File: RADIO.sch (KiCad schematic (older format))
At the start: 20 parts, among them Q501 MMBF170, U501 SN74AVC2T244, U502 SN74AVC2T244, U503 SN74AVC2T244, U504 A7, U505 SIM_SLOT, U506 SN74AVC2T244

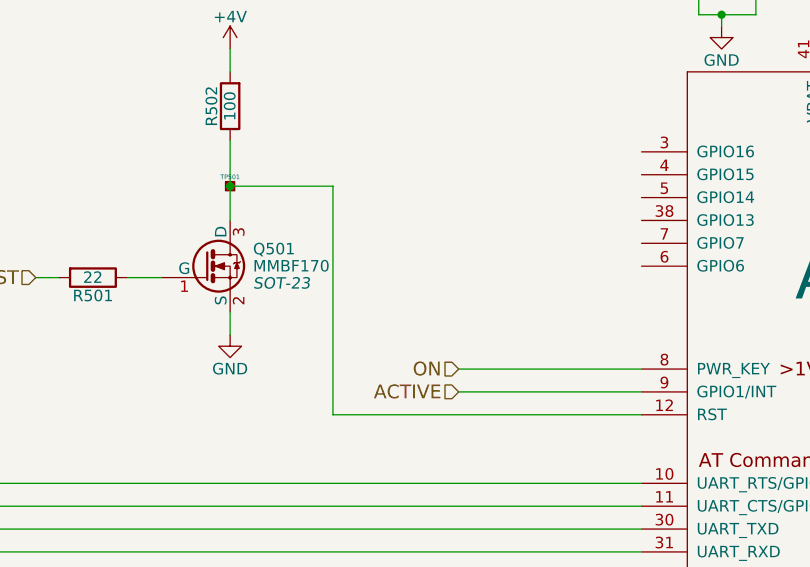
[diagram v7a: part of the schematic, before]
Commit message: Created netlist with current components Foreward Annotation to Board
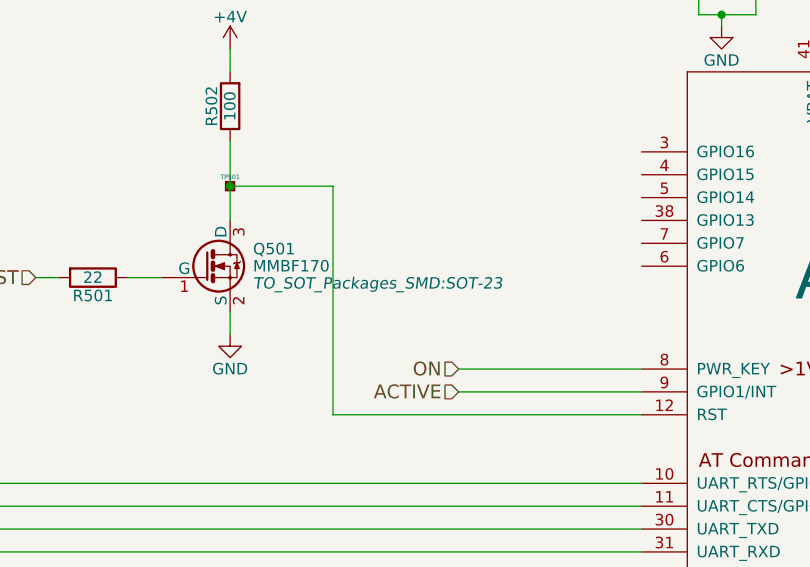
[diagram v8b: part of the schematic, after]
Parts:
- C501, C503, C504, C505, C506, C507: footprint Capacitors_SMD:C_0603 -> Capacitors_SMD:C_0402
- Q501: footprint SOT-23 -> TO_SOT_Packages_SMD:SOT-23
- R501, R502, R503, R504, R505: footprint Resistors_SMD:R_0603 -> Resistors_SMD:R_0402
- TP501: footprint buttons:TP -> NokiaRetroFit:TP
- U504: footprint buttons:A7 -> NokiaRetroFit:A7
- U505: footprint buttons:SIM -> NokiaRetroFit:SIM
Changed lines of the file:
@@
 F 0 "U504" H 10300 5750 60  0000 C CNN
 F 1 "A7" H 9700 4950 197 0000 C CNN
-F 2 "buttons:A7" H 9450 4650 60  0001 C CNN
+F 2 "NokiaRetroFit:A7" H 9450 4650 60  0001 C CNN
 F 3 "" H 9450 4650 60  0000 C CNN
 	1    9700 4450
@@
 F 0 "R501" V 6530 3950 50  0000 C CNN
 F 1 "22" V 6450 3950 50  0000 C CNN
-F 2 "Resistors_SMD:R_0603" V 6380 3950 50  0001 C CNN
+F 2 "Resistors_SMD:R_0402" V 6380 3950 50  0001 C CNN
 F 3 "" H 6450 3950 50  0000 C CNN
 	1    6450 3950
@@
 F 0 "R502" V 7130 3200 50  0000 C CNN
 F 1 "100" V 7050 3200 50  0000 C CNN
-F 2 "Resistors_SMD:R_0603" V 6980 3200 50  0001 C CNN
+F 2 "Resistors_SMD:R_0402" V 6980 3200 50  0001 C CNN
 F 3 "" H 7050 3200 50  0000 C CNN
 	1    7050 3200
@@
 F 0 "R504" V 11480 3900 50  0000 C CNN
 F 1 "0" V 11400 3900 50  0000 C CNN
-F 2 "Resistors_SMD:R_0603" V 11330 3900 50  0001 C CNN
+F 2 "Resistors_SMD:R_0402" V 11330 3900 50  0001 C CNN
 F 3 "" H 11400 3900 50  0000 C CNN
 	1    11400 3900
@@
 F 0 "C505" H 11160 4170 50  0000 L CNN
 F 1 "C" H 11160 4020 50  0000 L CNN
-F 2 "Capacitors_SMD:C_0603" H 11150 4100 50  0001 C CNN
+F 2 "Capacitors_SMD:C_0402" H 11150 4100 50  0001 C CNN
 F 3 "" H 11150 4100 50  0000 C CNN
 	1    11150 4100
@@
 F 0 "C507" H 11660 4170 50  0000 L CNN
 F 1 "C" H 11660 4020 50  0000 L CNN
-F 2 "Capacitors_SMD:C_0603" H 11650 4100 50  0001 C CNN
+F 2 "Capacitors_SMD:C_0402" H 11650 4100 50  0001 C CNN
 F 3 "" H 11650 4100 50  0000 C CNN
 	1    11650 4100
@@
 F 0 "R503" V 11480 3000 50  0000 C CNN
 F 1 "0" V 11400 3000 50  0000 C CNN
-F 2 "Resistors_SMD:R_0603" V 11330 3000 50  0001 C CNN
+F 2 "Resistors_SMD:R_0402" V 11330 3000 50  0001 C CNN
 F 3 "" H 11400 3000 50  0000 C CNN
 	1    11400 3000
@@
 F 0 "C504" H 11160 3270 50  0000 L CNN
 F 1 "C" H 11160 3120 50  0000 L CNN
-F 2 "Capacitors_SMD:C_0603" H 11150 3200 50  0001 C CNN
+F 2 "Capacitors_SMD:C_0402" H 11150 3200 50  0001 C CNN
 F 3 "" H 11150 3200 50  0000 C CNN
 	1    11150 3200
@@
 F 0 "C506" H 11660 3270 50  0000 L CNN
 F 1 "C" H 11660 3120 50  0000 L CNN
-F 2 "Capacitors_SMD:C_0603" H 11650 3200 50  0001 C CNN
+F 2 "Capacitors_SMD:C_0402" H 11650 3200 50  0001 C CNN
 F 3 "" H 11650 3200 50  0000 C CNN
 	1    11650 3200
@@
 F 0 "C501" H 9110 2670 50  0000 L CNN
 F 1 "100n" H 9110 2520 50  0000 L CNN
-F 2 "Capacitors_SMD:C_0603" H 9100 2600 50  0001 C CNN
+F 2 "Capacitors_SMD:C_0402" H 9100 2600 50  0001 C CNN
 F 3 "" H 9100 2600 50  0000 C CNN
 	1    9100 2600
@@
 F 0 "U505" H 12900 4950 60  0000 C CNN
 F 1 "SIM_SLOT" H 12900 4450 60  0000 C CNN
-F 2 "buttons:SIM" H 13050 4700 60  0001 C CNN
+F 2 "NokiaRetroFit:SIM" H 13050 4700 60  0001 C CNN
 F 3 "" H 13050 4700 60  0000 C CNN
 	1    13050 4700
@@
 F 0 "C503" H 10010 2670 50  0000 L CNN
 F 1 "100n" H 10010 2520 50  0000 L CNN
-F 2 "Capacitors_SMD:C_0603" H 10000 2600 50  0001 C CNN
+F 2 "Capacitors_SMD:C_0402" H 10000 2600 50  0001 C CNN
 F 3 "" H 10000 2600 50  0000 C CNN
 	1    10000 2600
@@
 F 0 "R505" V 13830 2850 50  0000 C CNN
 F 1 "100" V 13750 2850 50  0000 C CNN
-F 2 "Resistors_SMD:R_0603" V 13680 2850 50  0001 C CNN
+F 2 "Resistors_SMD:R_0402" V 13680 2850 50  0001 C CNN
 F 3 "" H 13750 2850 50  0000 C CNN
 F 4 "DNP" V 13750 2850 60  0000 C CNN "manufacture"
@@
 F 0 "TP501" H 7050 3590 20  0000 C CNN
 F 1 "TP" H 7050 3500 60  0001 C CNN
-F 2 "buttons:TP" H 7050 3550 60  0001 C CNN
+F 2 "NokiaRetroFit:TP" H 7050 3550 60  0001 C CNN
 F 3 "" H 7050 3550 60  0000 C CNN
 	1    7050 3550
@@
 F 0 "Q501" H 7150 3975 50  0000 L CNN
 F 1 "MMBF170" H 7150 3900 50  0000 L CNN
-F 2 "SOT-23" H 7150 3825 50  0000 L CIN
+F 2 "TO_SOT_Packages_SMD:SOT-23" H 7150 3825 50  0000 L CIN
 F 3 "" H 6950 3900 50  0000 L CNN
 	1    6950 3900
@@
 	5100 4600 5100 4700
 $Comp
-L GND #PWR092
+L GND #PWR091
 U 1 1 594649AA
 P 5100 4700
-F 0 "#PWR092" H 5100 4450 50  0001 C CNN
+F 0 "#PWR091" H 5100 4450 50  0001 C CNN
 F 1 "GND" H 5100 4550 50  0000 C CNN
 F 2 "" H 5100 4700 50  0000 C CNN
@@
 $EndComp
 $Comp
-L NVCC_3V3 #PWR093
+L NVCC_3V3 #PWR092
 U 1 1 5946648C
 P 3900 4100
-F 0 "#PWR093" H 3900 3950 50  0001 C CNN
+F 0 "#PWR092" H 3900 3950 50  0001 C CNN
 F 1 "NVCC_3V3" H 3900 4250 50  0000 C CNN
 F 2 "" H 3900 4100 50  0001 C CNN
@@
 	3900 4600 3900 4700
 $Comp
-L GND #PWR094
+L GND #PWR093
 U 1 1 5946669C
 P 3900 4700
-F 0 "#PWR094" H 3900 4450 50  0001 C CNN
+F 0 "#PWR093" H 3900 4450 50  0001 C CNN
 F 1 "GND" H 3900 4550 50  0000 C CNN
 F 2 "" H 3900 4700 50  0000 C CNN
@@
 $EndComp
 $Comp
-L VLDO4_2V8 #PWR095
+L VLDO4_2V8 #PWR094
 U 1 1 594667FC
 P 5100 5350
-F 0 "#PWR095" H 5100 5200 50  0001 C CNN
+F 0 "#PWR094" H 5100 5200 50  0001 C CNN
 F 1 "VLDO4_2V8" H 5100 5500 50  0000 C CNN
 F 2 "" H 5100 5350 50  0001 C CNN
@@
 	5100 5850 5100 5950
 $Comp
-L GND #PWR096
+L GND #PWR095
 U 1 1 59466808
 P 5100 5950
-F 0 "#PWR096" H 5100 5700 50  0001 C CNN
+F 0 "#PWR095" H 5100 5700 50  0001 C CNN
 F 1 "GND" H 5100 5800 50  0000 C CNN
 F 2 "" H 5100 5950 50  0000 C CNN
@@
 $EndComp
 $Comp
-L NVCC_3V3 #PWR097
+L NVCC_3V3 #PWR096
 U 1 1 5946680E
 P 3900 5350
-F 0 "#PWR097" H 3900 5200 50  0001 C CNN
+F 0 "#PWR096" H 3900 5200 50  0001 C CNN
 F 1 "NVCC_3V3" H 3900 5500 50  0000 C CNN
 F 2 "" H 3900 5350 50  0001 C CNN
@@
 	3900 5850 3900 5950
 $Comp
-L GND #PWR098
+L GND #PWR097
 U 1 1 5946681A
 P 3900 5950
-F 0 "#PWR098" H 3900 5700 50  0001 C CNN
+F 0 "#PWR097" H 3900 5700 50  0001 C CNN
 F 1 "GND" H 3900 5800 50  0000 C CNN
 F 2 "" H 3900 5950 50  0000 C CNN
@@
 $EndComp
 $Comp
-L VLDO4_2V8 #PWR099
+L VLDO4_2V8 #PWR098
 U 1 1 594A741B
 P 5100 6550
-F 0 "#PWR099" H 5100 6400 50  0001 C CNN
+F 0 "#PWR098" H 5100 6400 50  0001 C CNN
 F 1 "VLDO4_2V8" H 5100 6700 50  0000 C CNN
 F 2 "" H 5100 6550 50  0001 C CNN
@@
 	5100 7050 5100 7150
 $Comp
-L GND #PWR0100
+L GND #PWR099
 U 1 1 594A7427
 P 5100 7150
-F 0 "#PWR0100" H 5100 6900 50  0001 C CNN
+F 0 "#PWR099" H 5100 6900 50  0001 C CNN
 F 1 "GND" H 5100 7000 50  0000 C CNN
 F 2 "" H 5100 7150 50  0000 C CNN
@@
 $EndComp
 $Comp
-L NVCC_3V3 #PWR0101
+L NVCC_3V3 #PWR0100
 U 1 1 594A742D
 P 3900 6550
-F 0 "#PWR0101" H 3900 6400 50  0001 C CNN
+F 0 "#PWR0100" H 3900 6400 50  0001 C CNN
 F 1 "NVCC_3V3" H 3900 6700 50  0000 C CNN
 F 2 "" H 3900 6550 50  0001 C CNN
@@
 	3900 7050 3900 7150
 $Comp
-L GND #PWR0102
+L GND #PWR0101
 U 1 1 594A7439
 P 3900 7150
-F 0 "#PWR0102" H 3900 6900 50  0001 C CNN
+F 0 "#PWR0101" H 3900 6900 50  0001 C CNN
 F 1 "GND" H 3900 7000 50  0000 C CNN
 F 2 "" H 3900 7150 50  0000 C CNN
@@
 $EndComp
 $Comp
-L VLDO4_2V8 #PWR0103
+L VLDO4_2V8 #PWR0102
 U 1 1 594A9238
 P 13150 3200
-F 0 "#PWR0103" H 13150 3050 50  0001 C CNN
+F 0 "#PWR0102" H 13150 3050 50  0001 C CNN
 F 1 "VLDO4_2V8" H 13150 3350 50  0000 C CNN
 F 2 "" H 13150 3200 50  0001 C CNN
@@
 	13150 3700 13150 3800
 $Comp
-L GND #PWR0104
+L GND #PWR0103
 U 1 1 594A9244
 P 13150 3800
-F 0 "#PWR0104" H 13150 3550 50  0001 C CNN
+F 0 "#PWR0103" H 13150 3550 50  0001 C CNN
 F 1 "GND" H 13150 3650 50  0000 C CNN
 F 2 "" H 13150 3800 50  0000 C CNN
@@
 $EndComp
 $Comp
-L NVCC_3V3 #PWR0105
+L NVCC_3V3 #PWR0104
 U 1 1 594A924A
 P 14350 3200
-F 0 "#PWR0105" H 14350 3050 50  0001 C CNN
+F 0 "#PWR0104" H 14350 3050 50  0001 C CNN
 F 1 "NVCC_3V3" H 14350 3350 50  0000 C CNN
 F 2 "" H 14350 3200 50  0001 C CNN
@@
 	14350 3700 14350 3800
 $Comp
-L GND #PWR0106
+L GND #PWR0105
 U 1 1 594A9254
 P 14350 3800
-F 0 "#PWR0106" H 14350 3550 50  0001 C CNN
+F 0 "#PWR0105" H 14350 3550 50  0001 C CNN
 F 1 "GND" H 14350 3650 50  0000 C CNN
 F 2 "" H 14350 3800 50  0000 C CNN
@@
 	10600 4300 11950 4300
 $Comp
-L NVCC_1V8 #PWR0107
+L NVCC_1V8 #PWR0106
 U 1 1 594AAC99
 P 9800 2250
-F 0 "#PWR0107" H 9800 2100 50  0001 C CNN
+F 0 "#PWR0106" H 9800 2100 50  0001 C CNN
 F 1 "NVCC_1V8" H 9800 2400 50  0000 C CNN
 F 2 "" H 9800 2250 50  0001 C CNN
@@
 $EndComp
 $Comp
-L VLDO4_2V8 #PWR?
+L VLDO4_2V8 #PWR0107
 U 1 1 5962C5A0
 P 5100 4100
-F 0 "#PWR?" H 5100 3950 50  0001 C CNN
+F 0 "#PWR0107" H 5100 3950 50  0001 C CNN
 F 1 "VLDO4_2V8" H 5100 4250 50  0000 C CNN
 F 2 "" H 5100 4100 50  0001 C CNN
